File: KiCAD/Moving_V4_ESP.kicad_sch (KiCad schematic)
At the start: 88 parts, among them J1 Vin_1, J10 IO27_GPIO1, J11 IO32_GPIO2, J12 IO5_GPIO3(PU), J2 Power_SW, J3 Vin_XT, J4 USB_B_Micro, J5 Encorder_L, J6 Encorder_R, J7 MOTOR_L, J8 MOTOR_R, J9 IO4_GPIO0, Q1 U4_ALT2, Q2 U4_ALT2, Q3 U4_ALT2, U1 SE8650K2B-HF, U10 ITR8307-S17-TR8, U2 CH340X, U3 UZ1085L-33-TN3-R, U4 TXB0104RUT, U5 CP3119MDTR, U6 CP3119MDTR, U7 ESP32-WROOM-32, U8 ITR8307-S17-TR8, U9 ITR8307-S17-TR8

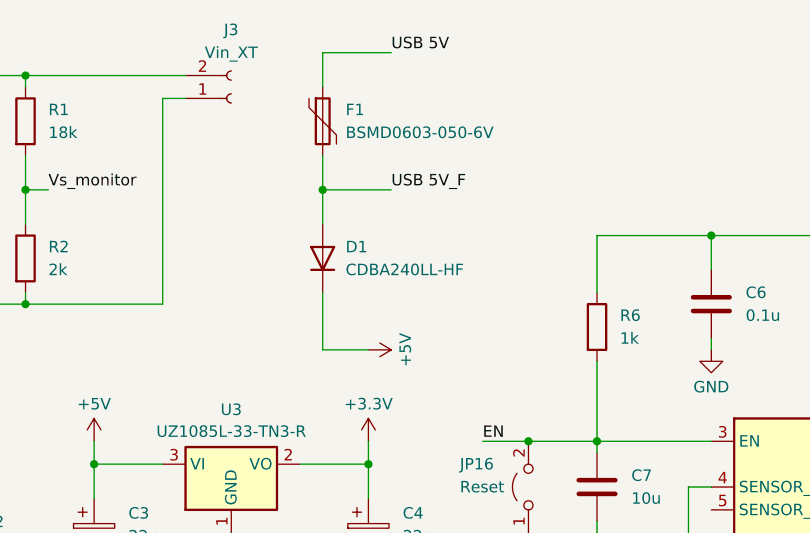
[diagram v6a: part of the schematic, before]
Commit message: USB電源でモータを回すためのジャンパを追加
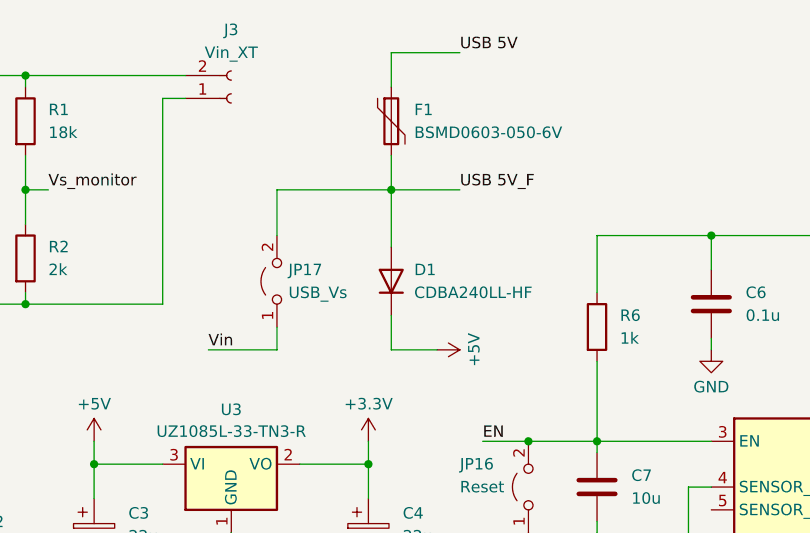
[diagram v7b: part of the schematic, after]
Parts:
- added JP17: USB_Vs, Jumper:SolderJumper-2_P1.3mm_Open_RoundedPad1.0x1.5mm, symbol Jumper:Jumper_2_Open
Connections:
- net USB 5V_F: now also JP17.2 (B)
- net Vin: now also JP17.1 (A)
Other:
- moved on the sheet: D1, F1
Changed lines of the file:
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@@
   (junction (at 63.5 63.5) (diameter 0) (color 0 0 0 0)
   )
-  (junction (at 88.9 33.02) (diameter 0) (color 0 0 0 0)
+  (junction (at 96.52 33.02) (diameter 0) (color 0 0 0 0)
   )
   (junction (at 55.88 33.02) (diameter 0) (color 0 0 0 0)
@@
     (stroke (width 0) (type default))
   )
-  (wire (pts (xy 88.9 29.21) (xy 88.9 33.02))
+  (wire (pts (xy 96.52 29.21) (xy 96.52 33.02))
     (stroke (width 0) (type default))
   )
@@
     (stroke (width 0) (type default))
   )
-  (wire (pts (xy 88.9 50.8) (xy 93.98 50.8))
+  (wire (pts (xy 96.52 50.8) (xy 101.6 50.8))
     (stroke (width 0) (type default))
   )
@@
     (stroke (width 0) (type default))
   )
-  (wire (pts (xy 88.9 17.78) (xy 88.9 21.59))
+  (wire (pts (xy 96.52 17.78) (xy 96.52 21.59))
     (stroke (width 0) (type default))
   )
@@
     (stroke (width 0) (type default))
   )
+  (wire (pts (xy 76.2 50.8) (xy 83.82 50.8))
+    (stroke (width 0) (type default))
+  )
   (wire (pts (xy 93.98 142.24) (xy 93.98 149.86))
     (stroke (width 0) (type default))
   )
-  (wire (pts (xy 96.52 17.78) (xy 88.9 17.78))
+  (wire (pts (xy 104.14 17.78) (xy 96.52 17.78))
     (stroke (width 0) (type default))
   )
@@
     (stroke (width 0) (type default))
   )
+  (wire (pts (xy 83.82 33.02) (xy 96.52 33.02))
+    (stroke (width 0) (type default))
+  )
   (wire (pts (xy 200.66 25.4) (xy 204.47 25.4))
     (stroke (width 0) (type default))
@@
     (stroke (width 0) (type default))
   )
-  (wire (pts (xy 96.52 33.02) (xy 88.9 33.02))
+  (wire (pts (xy 104.14 33.02) (xy 96.52 33.02))
     (stroke (width 0) (type default))
   )
@@
     (stroke (width 0) (type default))
   )
+  (wire (pts (xy 83.82 38.1) (xy 83.82 33.02))
+    (stroke (width 0) (type default))
+  )
   (wire (pts (xy 17.78 63.5) (xy 25.4 63.5))
     (stroke (width 0) (type default))
@@
     (stroke (width 0) (type default))
   )
-  (wire (pts (xy 88.9 33.02) (xy 88.9 36.83))
+  (wire (pts (xy 96.52 33.02) (xy 96.52 39.37))
     (stroke (width 0) (type default))
   )
@@
     (stroke (width 0) (type default))
   )
+  (wire (pts (xy 83.82 50.8) (xy 83.82 48.26))
+    (stroke (width 0) (type default))
+  )
   (wire (pts (xy 55.88 20.32) (xy 55.88 21.59))
     (stroke (width 0) (type default))
@@
     (stroke (width 0) (type default))
   )
-  (wire (pts (xy 88.9 44.45) (xy 88.9 50.8))
+  (wire (pts (xy 96.52 46.99) (xy 96.52 50.8))
     (stroke (width 0) (type default))
   )
@@
     (effects (font (size 1.27 1.27)) (justify left bottom))
   )
+  (label "Vin" (at 76.2 50.8 0) (fields_autoplaced)
+    (effects (font (size 1.27 1.27)) (justify left bottom))
+  )
   (label "SENSOR_1" (at 246.38 96.52 0) (fields_autoplaced)
     (effects (font (size 1.27 1.27)) (justify left bottom))
@@
     (effects (font (size 1.27 1.27)) (justify left bottom))
   )
-  (label "USB 5V_F" (at 96.52 33.02 0) (fields_autoplaced)
+  (label "USB 5V_F" (at 104.14 33.02 0) (fields_autoplaced)
     (effects (font (size 1.27 1.27)) (justify left bottom))
   )
@@
     (effects (font (size 1.27 1.27)) (justify left bottom))
   )
-  (label "USB 5V" (at 96.52 17.78 0) (fields_autoplaced)
+  (label "USB 5V" (at 104.14 17.78 0) (fields_autoplaced)
     (effects (font (size 1.27 1.27)) (justify left bottom))
   )
@@
     )
   )
+  (symbol (lib_id "Jumper:Jumper_2_Open") (at 83.82 43.18 90) (unit 1)
+    (in_bom yes) (on_board yes) (dnp no)
+    (property "Reference" "JP17" (at 85.09 41.91 90)
+      (effects (font (size 1.27 1.27)) (justify right))
+    )
+    (property "Value" "USB_Vs" (at 85.09 44.45 90)
+      (effects (font (size 1.27 1.27)) (justify right))
+    )
+    (property "Footprint" "Jumper:SolderJumper-2_P1.3mm_Open_RoundedPad1.0x1.5mm" (at 83.82 43.18 0)
+      (effects (font (size 1.27 1.27)) hide)
+    )
+    (property "Datasheet" "~" (at 83.82 43.18 0)
+      (effects (font (size 1.27 1.27)) hide)
+    )
+    (property "LCSC" "x" (at 83.82 43.18 0)
+      (effects (font (size 1.27 1.27)) hide)
+    )
+    (property "秋月" "x" (at 83.82 43.18 0)
+      (effects (font (size 1.27 1.27)) hide)
+    )
+    (pin "1")
+    (pin "2")
+    (instances
+      (project "Moving_V4_ESP"
+        (path "/515135d2-db88-48ff-b508-cbebeed2b019"
+          (reference "JP17") (unit 1)
+        )
+      )
+    )
+  )
   (symbol (lib_id "power:GND") (at 22.86 124.46 0) (unit 1)
     (in_bom yes) (on_board yes) (dnp no) (fields_autoplaced)
@@
     )
   )
-  (symbol (lib_id "Device:Polyfuse") (at 88.9 25.4 0) (unit 1)
-    (in_bom yes) (on_board yes) (dnp no) (fields_autoplaced)
-    (property "Reference" "F1" (at 91.44 24.13 0)
+  (symbol (lib_id "Device:Polyfuse") (at 96.52 25.4 0) (unit 1)
+    (in_bom yes) (on_board yes) (dnp no)
+    (property "Reference" "F1" (at 99.06 24.13 0)
       (effects (font (size 1.27 1.27)) (justify left))
     )
-    (property "Value" "BSMD0603-050-6V\n" (at 91.44 26.67 0)
+    (property "Value" "BSMD0603-050-6V\n" (at 99.06 26.67 0)
       (effects (font (size 1.27 1.27)) (justify left))
     )
-    (property "Footprint" "Fuse:Fuse_0603_1608Metric" (at 90.17 30.48 0)
+    (property "Footprint" "Fuse:Fuse_0603_1608Metric" (at 97.79 30.48 0)
       (effects (font (size 1.27 1.27)) (justify left) hide)
     )
-    (property "Datasheet" "~" (at 88.9 25.4 0)
+    (property "Datasheet" "~" (at 96.52 25.4 0)
       (effects (font (size 1.27 1.27)) hide)
     )
-    (property "LCSC" "C883095" (at 88.9 25.4 0)
+    (property "LCSC" "C883095" (at 96.52 25.4 0)
       (effects (font (size 1.27 1.27)) hide)
     )
-    (property "秋月" "" (at 88.9 25.4 0)
+    (property "秋月" "" (at 96.52 25.4 0)
       (effects (font (size 1.27 1.27)) hide)
     )
@@
     )
   )
-  (symbol (lib_id "Device:D") (at 88.9 40.64 90) (unit 1)
-    (in_bom yes) (on_board yes) (dnp no) (fields_autoplaced)
-    (property "Reference" "D1" (at 91.44 39.37 90)
+  (symbol (lib_id "Device:D") (at 96.52 43.18 90) (unit 1)
+    (in_bom yes) (on_board yes) (dnp no)
+    (property "Reference" "D1" (at 99.06 41.91 90)
       (effects (font (size 1.27 1.27)) (justify right))
     )
-    (property "Value" "CDBA240LL-HF" (at 91.44 41.91 90)
+    (property "Value" "CDBA240LL-HF" (at 99.06 44.45 90)
       (effects (font (size 1.27 1.27)) (justify right))
     )
-    (property "Footprint" "Diode_SMD:D_SMA" (at 88.9 40.64 0)
+    (property "Footprint" "Diode_SMD:D_SMA" (at 96.52 43.18 0)
       (effects (font (size 1.27 1.27)) hide)
     )
-    (property "Datasheet" "~" (at 88.9 40.64 0)
+    (property "Datasheet" "~" (at 96.52 43.18 0)
       (effects (font (size 1.27 1.27)) hide)
     )
-    (property "Sim.Device" "D" (at 88.9 40.64 0)
+    (property "Sim.Device" "D" (at 96.52 43.18 0)
       (effects (font (size 1.27 1.27)) hide)
     )
-    (property "Sim.Pins" "1=K 2=A" (at 88.9 40.64 0)
+    (property "Sim.Pins" "1=K 2=A" (at 96.52 43.18 0)
       (effects (font (size 1.27 1.27)) hide)
     )
-    (property "LCSC" "C2886093" (at 88.9 40.64 0)
+    (property "LCSC" "C2886093" (at 96.52 43.18 0)
       (effects (font (size 1.27 1.27)) hide)
     )
-    (property "秋月" "" (at 88.9 40.64 0)
+    (property "秋月" "" (at 96.52 43.18 0)
       (effects (font (size 1.27 1.27)) hide)
     )
@@
     )
   )
-  (symbol (lib_id "power:+5V") (at 93.98 50.8 270) (unit 1)
+  (symbol (lib_id "power:+5V") (at 101.6 50.8 270) (unit 1)
     (in_bom yes) (on_board yes) (dnp no) (fields_autoplaced)
-    (property "Reference" "#PWR017" (at 90.17 50.8 0)
+    (property "Reference" "#PWR017" (at 97.79 50.8 0)
       (effects (font (size 1.27 1.27)) hide)
     )
-    (property "Value" "+5V" (at 98.1131 50.8 0)
+    (property "Value" "+5V" (at 105.7331 50.8 0)
       (effects (font (size 1.27 1.27)))
     )
-    (property "Footprint" "" (at 93.98 50.8 0)
+    (property "Footprint" "" (at 101.6 50.8 0)
       (effects (font (size 1.27 1.27)) hide)
     )
-    (property "Datasheet" "" (at 93.98 50.8 0)
+    (property "Datasheet" "" (at 101.6 50.8 0)
       (effects (font (size 1.27 1.27)) hide)
     )

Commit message: リセット用じジャンパをSMDスイッチが取り付けできる形に変更
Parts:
- JP16: footprint Jumper:SolderJumper-2_P1.3mm_Open_RoundedPad1.0x1.5mm -> YY_Common:SolderJumper-2_TVAF06-A020B-R_COMPATIBLE; 秋月 x -> 114888
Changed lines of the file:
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@@
       (effects (font (size 1.27 1.27)) (justify right))
     )
-    (property "Footprint" "Jumper:SolderJumper-2_P1.3mm_Open_RoundedPad1.0x1.5mm" (at 111.76 66.04 0)
+    (property "Footprint" "YY_Common:SolderJumper-2_TVAF06-A020B-R_COMPATIBLE" (at 111.76 66.04 0)
       (effects (font (size 1.27 1.27)) hide)
     )
@@
       (effects (font (size 1.27 1.27)) hide)
     )
-    (property "秋月" "x" (at 111.76 66.04 0)
+    (property "秋月" "114888" (at 111.76 66.04 0)
       (effects (font (size 1.27 1.27)) hide)
     )
